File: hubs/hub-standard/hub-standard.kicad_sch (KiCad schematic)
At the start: 46 parts, among them J1 5VSB_IN, J2 PORT1, J3 PORT2, J4 PORT3, J5 PORT4, J6 USB-C, SW1 SW_RST, SW2 SW_BOOT, U1 ESP32-S3-WROOM-1, U2 TJA1462A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

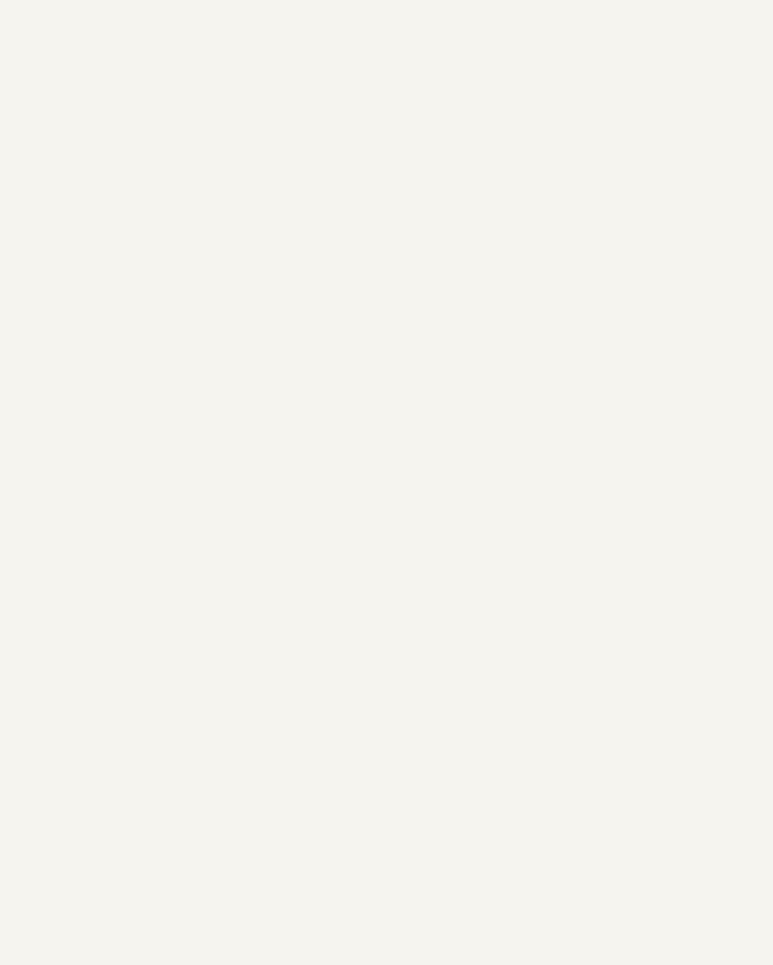
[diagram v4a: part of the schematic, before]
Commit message: hub-standard: add 4x DETECT pin-8 ESD diodes (D2-D5)
Platform-wide v3.2 board change (spec §2.4 v2.0): one low-capacitance ESD diode
on each DETECT line for hot-plug insertion ESD on the bare ESP32 ADC input. The
Hub has 4 DETECT lines (one per RJ-45 port), so 4 diodes:
  DETECT1->D2, DETECT2->D3, DETECT3->D4, DETECT4->D5; anodes to GND.
Footprint cec-Diode_SMD:D_SOD-323; SB120 body stand-in (already in this board's
lib_symbols cache), value PESD5V0S1UL. Placed on-grid, connected via short wire
stubs (cathode -> DETECTn label, anode -> GND). ERC 0 errors.

No Hub poke-and-ack hardware: the Hub pokes each DETECT line in firmware via the
existing ADC GPIO (brief-drive method); the switchable-pull-up vs brief-drive
choice is OQ-28, and brief-drive needs no extra parts.

https://claude.ai/code/session_01JVK4H2BFfihS7YDieYFgcV
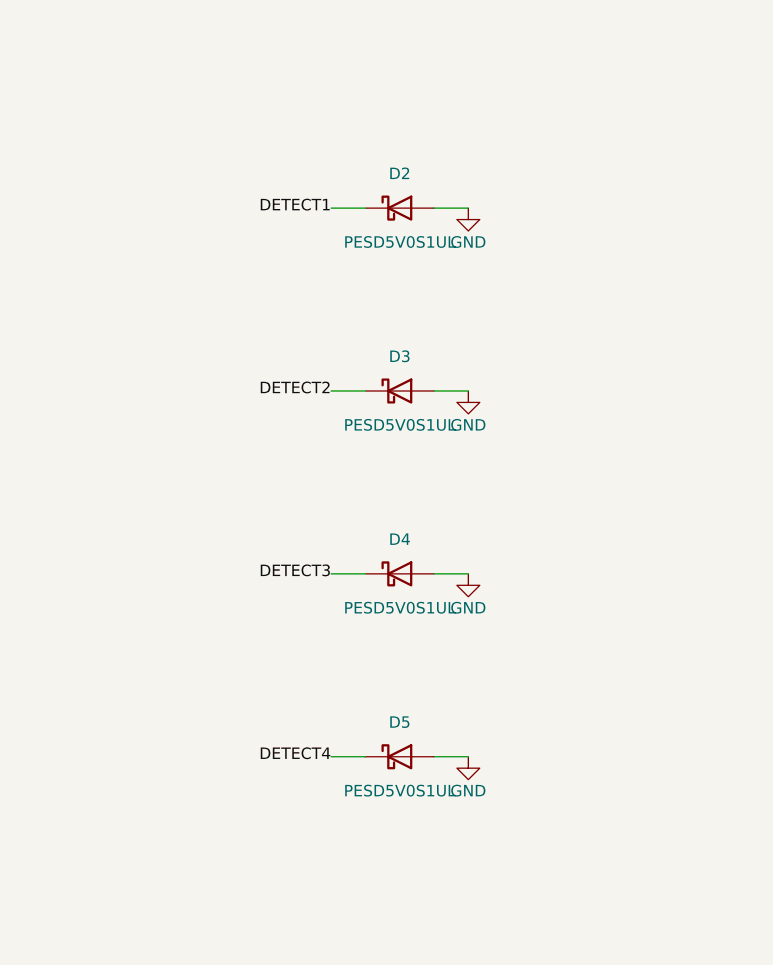
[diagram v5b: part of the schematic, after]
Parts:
- added D2, D3, D4, D5: PESD5V0S1UL, cec-Diode_SMD:D_SOD-323, symbol cec-vendor:SB120
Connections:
- net DETECT1: now also D2.1 (K)
- net DETECT2: now also D3.1 (K)
- net DETECT3: now also D4.1 (K)
- net DETECT4: now also D5.1 (K)
- net GND: now also D2.2 (A), D3.2 (A), D4.2 (A), D5.2 (A)
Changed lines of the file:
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@@
 		)
+	)
+	(symbol
+		(lib_id "cec-vendor:SB120")
+		(at 76.2 118.11 0)
+		(unit 1)(body_style 1)(exclude_from_sim no)(in_bom yes)(on_board yes)(in_pos_files yes)(dnp no)
+		(property "Reference" "D2" (at 76.2 114.3 0)(show_name no)(do_not_autoplace no)(effects (font (size 1.27 1.27))))
+		(property "Value" "PESD5V0S1UL" (at 76.2 121.92 0)(show_name no)(do_not_autoplace no)(effects (font (size 1.27 1.27))))
+		(property "Footprint" "cec-Diode_SMD:D_SOD-323" (at 76.2 118.11 0)(hide yes)(show_name no)(do_not_autoplace no)(effects (font (size 1.27 1.27))))
+		(property "Datasheet" "" (at 76.2 118.11 0)(hide yes)(show_name no)(do_not_autoplace no)(effects (font (size 1.27 1.27))))
+		(property "Description" "Low-cap DETECT ESD diode (pin8 hot-plug, spec 2.4 v2.0)" (at 76.2 118.11 0)(hide yes)(show_name no)(do_not_autoplace no)(effects (font (size 1.27 1.27))))
+		(pin "1")
+		(pin "2")
+		(instances (project "hub-standard" (path "/aa22b2b4-0e2b-481a-a188-ee3f43fcbaa8" (reference "D2") (unit 1))))
+	)
+	(wire (pts (xy 72.39 118.11) (xy 68.58 118.11)) (stroke (width 0) (type default)))
+	(label "DETECT1" (at 68.58 118.11 0) (effects (font (size 1.27 1.27)) (justify right)))
+	(wire (pts (xy 80.01 118.11) (xy 83.82 118.11)) (stroke (width 0) (type default)))
+	(symbol
+		(lib_id "cec-power:GND")
+		(at 83.82 118.11 0)
+		(unit 1)(body_style 1)(exclude_from_sim no)(in_bom yes)(on_board yes)(in_pos_files yes)(dnp no)
+		(property "Reference" "#PWR0301" (at 83.82 123.19 0)(hide yes)(show_name no)(do_not_autoplace no)(effects (font (size 1.27 1.27))))
+		(property "Value" "GND" (at 83.82 121.92 0)(show_name no)(do_not_autoplace no)(effects (font (size 1.27 1.27))))
+		(property "Footprint" "" (at 83.82 118.11 0)(show_name no)(do_not_autoplace no)(effects (font (size 1.27 1.27))))
+		(property "Datasheet" "" (at 83.82 118.11 0)(show_name no)(do_not_autoplace no)(effects (font (size 1.27 1.27))))
+		(property "Description" "" (at 83.82 118.11 0)(show_name no)(do_not_autoplace no)(effects (font (size 1.27 1.27))))
+		(pin "1")
+		(instances (project "hub-standard" (path "/aa22b2b4-0e2b-481a-a188-ee3f43fcbaa8" (reference "#PWR0301") (unit 1))))
+	)
+	(symbol
+		(lib_id "cec-vendor:SB120")
+		(at 76.2 138.43 0)
+		(unit 1)(body_style 1)(exclude_from_sim no)(in_bom yes)(on_board yes)(in_pos_files yes)(dnp no)
+		(property "Reference" "D3" (at 76.2 134.62 0)(show_name no)(do_not_autoplace no)(effects (font (size 1.27 1.27))))
+		(property "Value" "PESD5V0S1UL" (at 76.2 142.24 0)(show_name no)(do_not_autoplace no)(effects (font (size 1.27 1.27))))
+		(property "Footprint" "cec-Diode_SMD:D_SOD-323" (at 76.2 138.43 0)(hide yes)(show_name no)(do_not_autoplace no)(effects (font (size 1.27 1.27))))
+		(property "Datasheet" "" (at 76.2 138.43 0)(hide yes)(show_name no)(do_not_autoplace no)(effects (font (size 1.27 1.27))))
+		(property "Description" "Low-cap DETECT ESD diode (pin8 hot-plug, spec 2.4 v2.0)" (at 76.2 138.43 0)(hide yes)(show_name no)(do_not_autoplace no)(effects (font (size 1.27 1.27))))
+		(pin "1")
+		(pin "2")
+		(instances (project "hub-standard" (path "/aa22b2b4-0e2b-481a-a188-ee3f43fcbaa8" (reference "D3") (unit 1))))
+	)
+	(wire (pts (xy 72.39 138.43) (xy 68.58 138.43)) (stroke (width 0) (type default)))
+	(label "DETECT2" (at 68.58 138.43 0) (effects (font (size 1.27 1.27)) (justify right)))
+	(wire (pts (xy 80.01 138.43) (xy 83.82 138.43)) (stroke (width 0) (type default)))
+	(symbol
+		(lib_id "cec-power:GND")
+		(at 83.82 138.43 0)
+		(unit 1)(body_style 1)(exclude_from_sim no)(in_bom yes)(on_board yes)(in_pos_files yes)(dnp no)
+		(property "Reference" "#PWR0302" (at 83.82 143.51 0)(hide yes)(show_name no)(do_not_autoplace no)(effects (font (size 1.27 1.27))))
+		(property "Value" "GND" (at 83.82 142.24 0)(show_name no)(do_not_autoplace no)(effects (font (size 1.27 1.27))))
+		(property "Footprint" "" (at 83.82 138.43 0)(show_name no)(do_not_autoplace no)(effects (font (size 1.27 1.27))))
+		(property "Datasheet" "" (at 83.82 138.43 0)(show_name no)(do_not_autoplace no)(effects (font (size 1.27 1.27))))
+		(property "Description" "" (at 83.82 138.43 0)(show_name no)(do_not_autoplace no)(effects (font (size 1.27 1.27))))
+		(pin "1")
+		(instances (project "hub-standard" (path "/aa22b2b4-0e2b-481a-a188-ee3f43fcbaa8" (reference "#PWR0302") (unit 1))))
+	)
+	(symbol
+		(lib_id "cec-vendor:SB120")
+		(at 76.2 158.75 0)
+		(unit 1)(body_style 1)(exclude_from_sim no)(in_bom yes)(on_board yes)(in_pos_files yes)(dnp no)
+		(property "Reference" "D4" (at 76.2 154.94 0)(show_name no)(do_not_autoplace no)(effects (font (size 1.27 1.27))))
+		(property "Value" "PESD5V0S1UL" (at 76.2 162.56 0)(show_name no)(do_not_autoplace no)(effects (font (size 1.27 1.27))))
+		(property "Footprint" "cec-Diode_SMD:D_SOD-323" (at 76.2 158.75 0)(hide yes)(show_name no)(do_not_autoplace no)(effects (font (size 1.27 1.27))))
+		(property "Datasheet" "" (at 76.2 158.75 0)(hide yes)(show_name no)(do_not_autoplace no)(effects (font (size 1.27 1.27))))
+		(property "Description" "Low-cap DETECT ESD diode (pin8 hot-plug, spec 2.4 v2.0)" (at 76.2 158.75 0)(hide yes)(show_name no)(do_not_autoplace no)(effects (font (size 1.27 1.27))))
+		(pin "1")
+		(pin "2")
+		(instances (project "hub-standard" (path "/aa22b2b4-0e2b-481a-a188-ee3f43fcbaa8" (reference "D4") (unit 1))))
+	)
+	(wire (pts (xy 72.39 158.75) (xy 68.58 158.75)) (stroke (width 0) (type default)))
+	(label "DETECT3" (at 68.58 158.75 0) (effects (font (size 1.27 1.27)) (justify right)))
+	(wire (pts (xy 80.01 158.75) (xy 83.82 158.75)) (stroke (width 0) (type default)))
+	(symbol
+		(lib_id "cec-power:GND")
+		(at 83.82 158.75 0)
+		(unit 1)(body_style 1)(exclude_from_sim no)(in_bom yes)(on_board yes)(in_pos_files yes)(dnp no)
+		(property "Reference" "#PWR0303" (at 83.82 163.83 0)(hide yes)(show_name no)(do_not_autoplace no)(effects (font (size 1.27 1.27))))
+		(property "Value" "GND" (at 83.82 162.56 0)(show_name no)(do_not_autoplace no)(effects (font (size 1.27 1.27))))
+		(property "Footprint" "" (at 83.82 158.75 0)(show_name no)(do_not_autoplace no)(effects (font (size 1.27 1.27))))
+		(property "Datasheet" "" (at 83.82 158.75 0)(show_name no)(do_not_autoplace no)(effects (font (size 1.27 1.27))))
+		(property "Description" "" (at 83.82 158.75 0)(show_name no)(do_not_autoplace no)(effects (font (size 1.27 1.27))))
+		(pin "1")
+		(instances (project "hub-standard" (path "/aa22b2b4-0e2b-481a-a188-ee3f43fcbaa8" (reference "#PWR0303") (unit 1))))
+	)
+	(symbol
+		(lib_id "cec-vendor:SB120")
+		(at 76.2 179.07 0)
+		(unit 1)(body_style 1)(exclude_from_sim no)(in_bom yes)(on_board yes)(in_pos_files yes)(dnp no)
+		(property "Reference" "D5" (at 76.2 175.26 0)(show_name no)(do_not_autoplace no)(effects (font (size 1.27 1.27))))
+		(property "Value" "PESD5V0S1UL" (at 76.2 182.88 0)(show_name no)(do_not_autoplace no)(effects (font (size 1.27 1.27))))
+		(property "Footprint" "cec-Diode_SMD:D_SOD-323" (at 76.2 179.07 0)(hide yes)(show_name no)(do_not_autoplace no)(effects (font (size 1.27 1.27))))
+		(property "Datasheet" "" (at 76.2 179.07 0)(hide yes)(show_name no)(do_not_autoplace no)(effects (font (size 1.27 1.27))))
+		(property "Description" "Low-cap DETECT ESD diode (pin8 hot-plug, spec 2.4 v2.0)" (at 76.2 179.07 0)(hide yes)(show_name no)(do_not_autoplace no)(effects (font (size 1.27 1.27))))
+		(pin "1")
+		(pin "2")
+		(instances (project "hub-standard" (path "/aa22b2b4-0e2b-481a-a188-ee3f43fcbaa8" (reference "D5") (unit 1))))
+	)
+	(wire (pts (xy 72.39 179.07) (xy 68.58 179.07)) (stroke (width 0) (type default)))
+	(label "DETECT4" (at 68.58 179.07 0) (effects (font (size 1.27 1.27)) (justify right)))
+	(wire (pts (xy 80.01 179.07) (xy 83.82 179.07)) (stroke (width 0) (type default)))
+	(symbol
+		(lib_id "cec-power:GND")
+		(at 83.82 179.07 0)
+		(unit 1)(body_style 1)(exclude_from_sim no)(in_bom yes)(on_board yes)(in_pos_files yes)(dnp no)
+		(property "Reference" "#PWR0304" (at 83.82 184.15 0)(hide yes)(show_name no)(do_not_autoplace no)(effects (font (size 1.27 1.27))))
+		(property "Value" "GND" (at 83.82 182.88 0)(show_name no)(do_not_autoplace no)(effects (font (size 1.27 1.27))))
+		(property "Footprint" "" (at 83.82 179.07 0)(show_name no)(do_not_autoplace no)(effects (font (size 1.27 1.27))))
+		(property "Datasheet" "" (at 83.82 179.07 0)(show_name no)(do_not_autoplace no)(effects (font (size 1.27 1.27))))
+		(property "Description" "" (at 83.82 179.07 0)(show_name no)(do_not_autoplace no)(effects (font (size 1.27 1.27))))
+		(pin "1")
+		(instances (project "hub-standard" (path "/aa22b2b4-0e2b-481a-a188-ee3f43fcbaa8" (reference "#PWR0304") (unit 1))))
 	)
 	(sheet_instances

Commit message: Initial board commit.
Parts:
- renumbered C_SS to C_SS1, C_bulk to C_bulk1, R_ILIM to R_ILIM1

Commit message: hub-standard: fix U4 (TPS3839) footprint SOT-23-5 -> SOT-23 (3-pin)
Re-applied on top of the "Initial board commit". "Update PCB from Schematic"
warned about no net for U4 pads 4/5 (no pin 4/5 in symbol): U4 is the TPS3839
supervisor, a 3-pin part (SOT-23/DBZ; symbol pins 1=GND, 2=RESET->EN, 3=VDD->
+3V3), but the footprint pass had assigned the 5-pad SOT-23-5.

Retargeted ONLY U4 to cec-Package_TO_SOT_SMD:SOT-23 (U3/LP5907 keeps SOT-23-5);
vendored the 3-pin SOT-23 footprint. ERC 0 errors. Re-run Update PCB from
Schematic to clear the two warnings.

https://claude.ai/code/session_01JVK4H2BFfihS7YDieYFgcV
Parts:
- U4: footprint cec-Package_TO_SOT_SMD:SOT-23-5 -> cec-Package_TO_SOT_SMD:SOT-23
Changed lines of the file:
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@@
 			)
 		)
-		(property "Footprint" "cec-Package_TO_SOT_SMD:SOT-23-5"
+		(property "Footprint" "cec-Package_TO_SOT_SMD:SOT-23"
 			(at 154.94 110.49 0)
 			(hide yes)

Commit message: hub-standard: fix D1 footprint (CI hygiene) + checklist build/ prune
The actual CI failure was the repo-hygiene check, not the DRC (the DRAFT
marker skips ERC/DRC). D1 was a stray through-hole Diode_THT:D_DO-41 carrying
a machine-global ${KICAD10_3DMODEL_DIR} 3D-model path (clone-parity violation),
with an empty footprint field in the schematic.

- Schematic: point D1 at the vendored cec-Diode_SMD:D_SMA (SMA, relative 3D
  model). Re-sync the PCB to swap D1 DO-41 -> SMA and re-route its two traces.
- PCB: strip the global 3D-model block from D1's footprint so hygiene passes now.
- checklist.sh: its global-path grep didn't prune build/ (gitignored), so it
  false-failed locally on the vendored kicad-libs; exclude build/ and .git to
  match the script's other checks.

CI hygiene passes; ERC/DRC remain DRAFT-skipped.
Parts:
- D1: footprint Diode_THT:D_DO-41_SOD81_P10.16mm_Horizontal -> cec-Diode_SMD:D_SMA
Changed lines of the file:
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@@
 			)
 		)
-		(property "Footprint" "Diode_THT:D_DO-41_SOD81_P10.16mm_Horizontal"
+		(property "Footprint" "cec-Diode_SMD:D_SMA"
 			(at 448.31 88.265 0)
 			(hide yes)
